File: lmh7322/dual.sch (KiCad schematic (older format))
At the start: 35 parts, among them U1 lmh7322

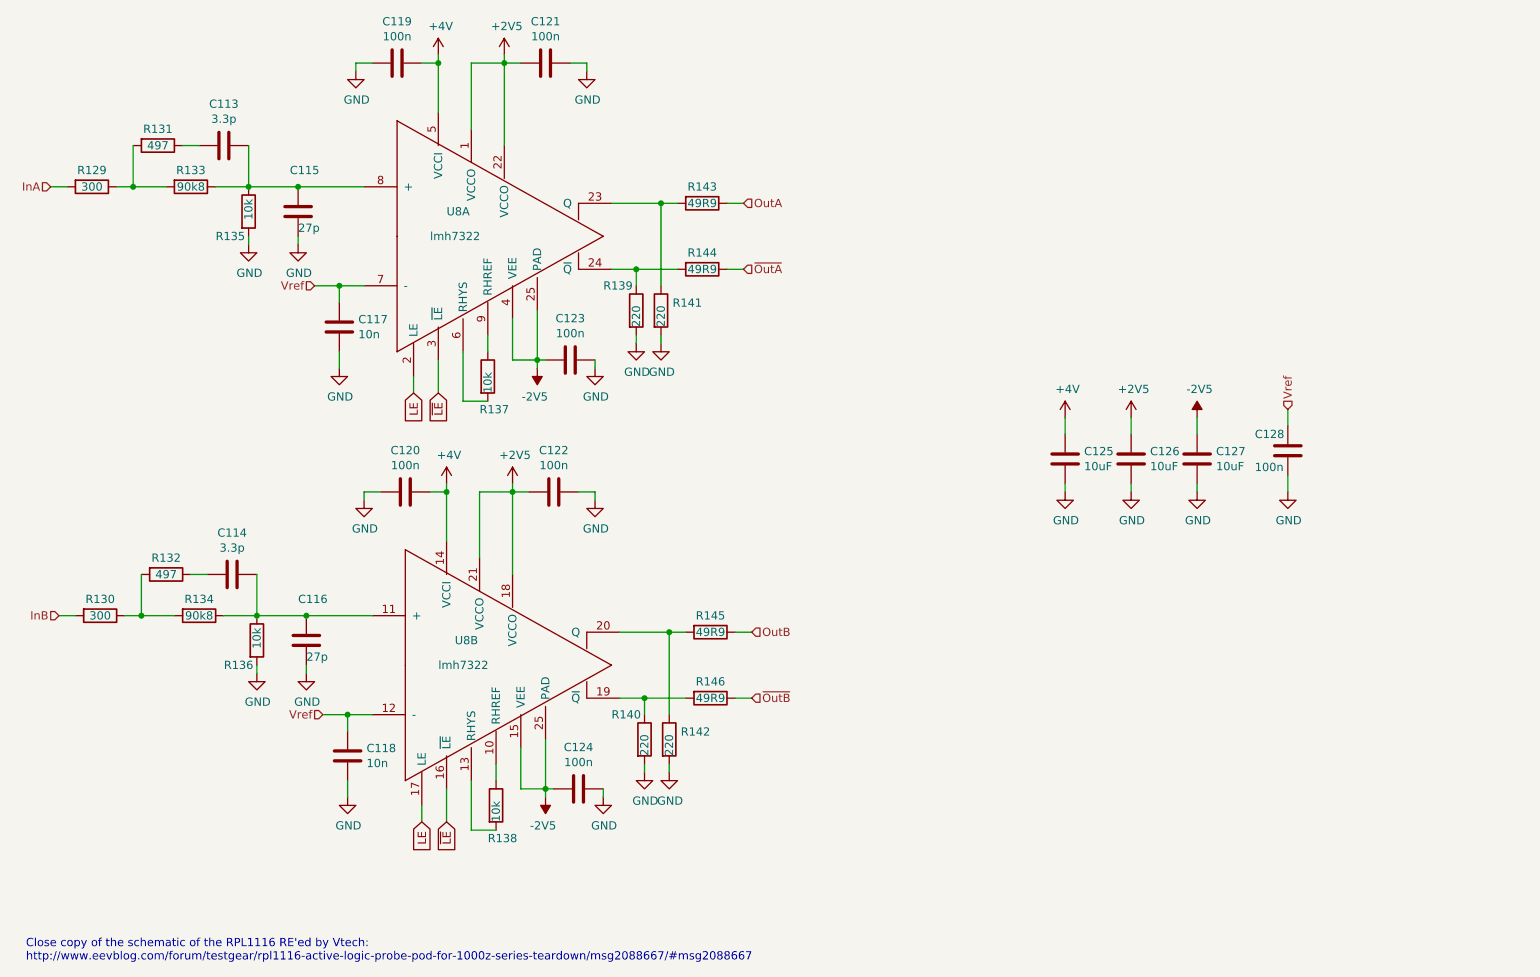
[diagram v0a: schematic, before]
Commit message: Use resistor arrays in the outputs
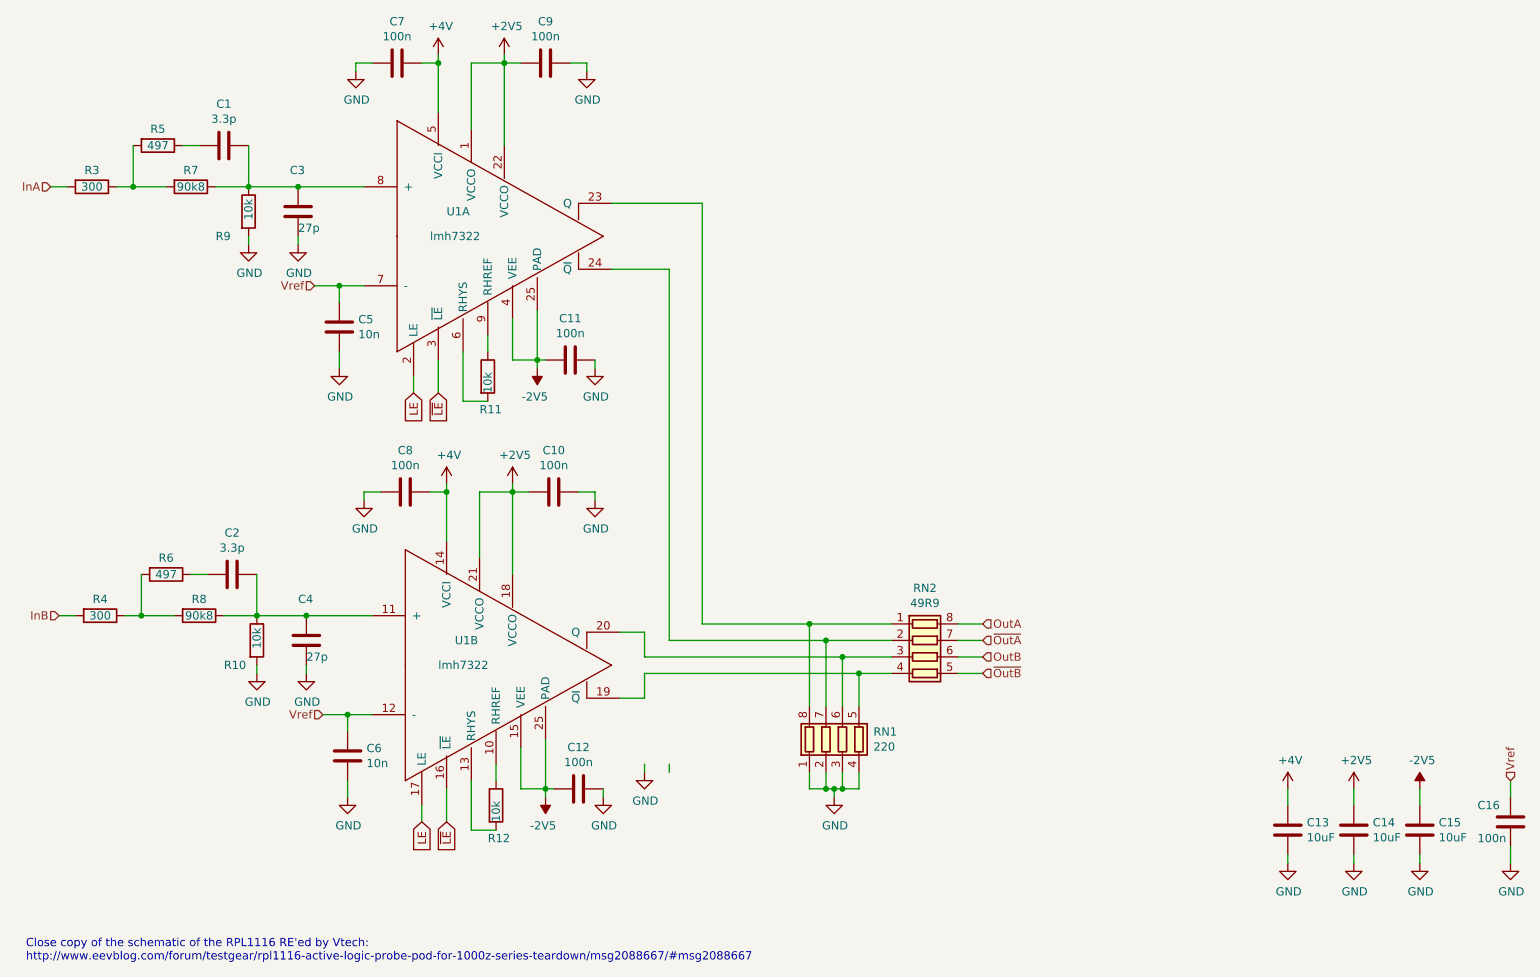
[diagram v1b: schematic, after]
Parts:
- removed R13, R14, R15, R16: 220, symbol Device:R
- removed R17, R18, R19, R20: 49R9, symbol Device:R
- added RN15: 220, symbol Device:R_Pack04
- added RN16: 49R9, symbol Device:R_Pack04
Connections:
- net GND: now also RN15.1 (R1.1), RN15.2 (R2.1), RN15.3 (R3.1), RN15.4 (R4.1)
- net OutA: now also RN16.8 (R1.2)
- net OutB: now also RN16.6 (R3.2)
- net ~OutA: now also RN16.7 (R2.2)
- net ~OutB: now also RN16.5 (R4.2)
- net at U1.23 (Q): now also RN15.8 (R1.2), RN16.1 (R1.1)
- net at U1.24 (~Q): now also RN15.7 (R2.2), RN16.2 (R2.1)
- net at U1.19 (~Q): now also RN15.5 (R4.2), RN16.4 (R4.1)
- net at U1.20 (Q): now also RN15.6 (R3.2), RN16.3 (R3.1)
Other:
- moved on the sheet: C13, C14, C15, C16

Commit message: Minor cleanup
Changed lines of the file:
@@
-$Comp
-L power:GND #PWR?
-U 1 1 5C467B73
-P 4900 5250
-AR Path="/5C467B73" Ref="#PWR?"  Part="1"
-AR Path="/5C4819A8/5C467B73" Ref="#PWR?"  Part="1"
-AR Path="/5C4C51E0/5C467B73" Ref="#PWR?"  Part="1"
-AR Path="/5C4E887D/5C467B73" Ref="#PWR?"  Part="1"
-AR Path="/5C4EBCE6/5C467B73" Ref="#PWR?"  Part="1"
-AR Path="/5C43A963/5C467B73" Ref="#PWR?"  Part="1"
-AR Path="/5C414CC7/5C467B73" Ref="#PWR039"  Part="1"
-AR Path="/5C4B42BD/5C467B73" Ref="#PWR068"  Part="1"
-AR Path="/5C4D3DE8/5C467B73" Ref="#PWR097"  Part="1"
-AR Path="/5C4DB186/5C467B73" Ref="#PWR0126"  Part="1"
-AR Path="/5C4E2524/5C467B73" Ref="#PWR0155"  Part="1"
-AR Path="/5C4E98BE/5C467B73" Ref="#PWR0184"  Part="1"
-AR Path="/5C4E98C7/5C467B73" Ref="#PWR0213"  Part="1"
-AR Path="/5C4E98D0/5C467B73" Ref="#PWR0242"  Part="1"
-F 0 "#PWR039" H 4900 5000 50  0001 C CNN
-F 1 "GND" H 4905 5077 50  0000 C CNN
-F 2 "" H 4900 5250 50  0001 C CNN
-F 3 "" H 4900 5250 50  0001 C CNN
-	1    4900 5250
-	1    0    0    -1
-$EndComp
 $Comp
 L power:GND #PWR?
@@
 	1    0    0    -1
 $EndComp
-Wire Wire Line
-	5050 5250 5050 5200
-Wire Wire Line
-	4900 5200 4900 5250
 Text HLabel 6950 4650 2    50   Input ~ 0
 ~OutB

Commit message: Started playing around with the PCB layout
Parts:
- removed C13, C14, C15: 10uF, symbol Device:C
- removed C16: 100n, symbol Device:C
- C1, C10, C11, C12, C2, C3, C4, C5, C6, C7, C8, C9: footprint (none) -> Capacitors_SMD.pretty:C_0603_HandSoldering
- R10, R11, R12, R3, R4, R5, R6, R7, R8, R9: footprint (none) -> Resistor_SMD:R_0603_1608Metric_Pad1.05x0.95mm_HandSolder
- RN15, RN16: footprint (none) -> Resistor_SMD:R_Array_Convex_4x0603
- U1: footprint (none) -> Package_DFN_QFN:QFN-24-1EP_4x4mm_P0.5mm_EP2.6x2.6mm_ThermalVias
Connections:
- net OutA: now also RN16.7 (R2.2); no longer RN16.8 (R1.2)
- net ~OutA: now also RN16.8 (R1.2); no longer RN16.7 (R2.2)
- net at RN15.8 (R1.2), RN16.1 (R1.1): now also U1.24 (~Q); no longer U1.23 (Q)
- net at RN15.7 (R2.2), RN16.2 (R2.1): now also U1.23 (Q); no longer U1.24 (~Q)

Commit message: Pre-clone
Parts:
- renumbered C1 to C201, C2 to C202, C3 to C203, C4 to C204, C5 to C205, C6 to C206, C7 to C207, C8 to C208, C9 to C209, C10 to C210, C11 to C211, C12 to C212, R3 to R201, R4 to R202, R5 to R203, R6 to R204, R7 to R205, R8 to R206, R9 to R207, R10 to R208, R11 to R209, R12 to R210, RN15 to RN901, RN16 to RN902, U1 to U201

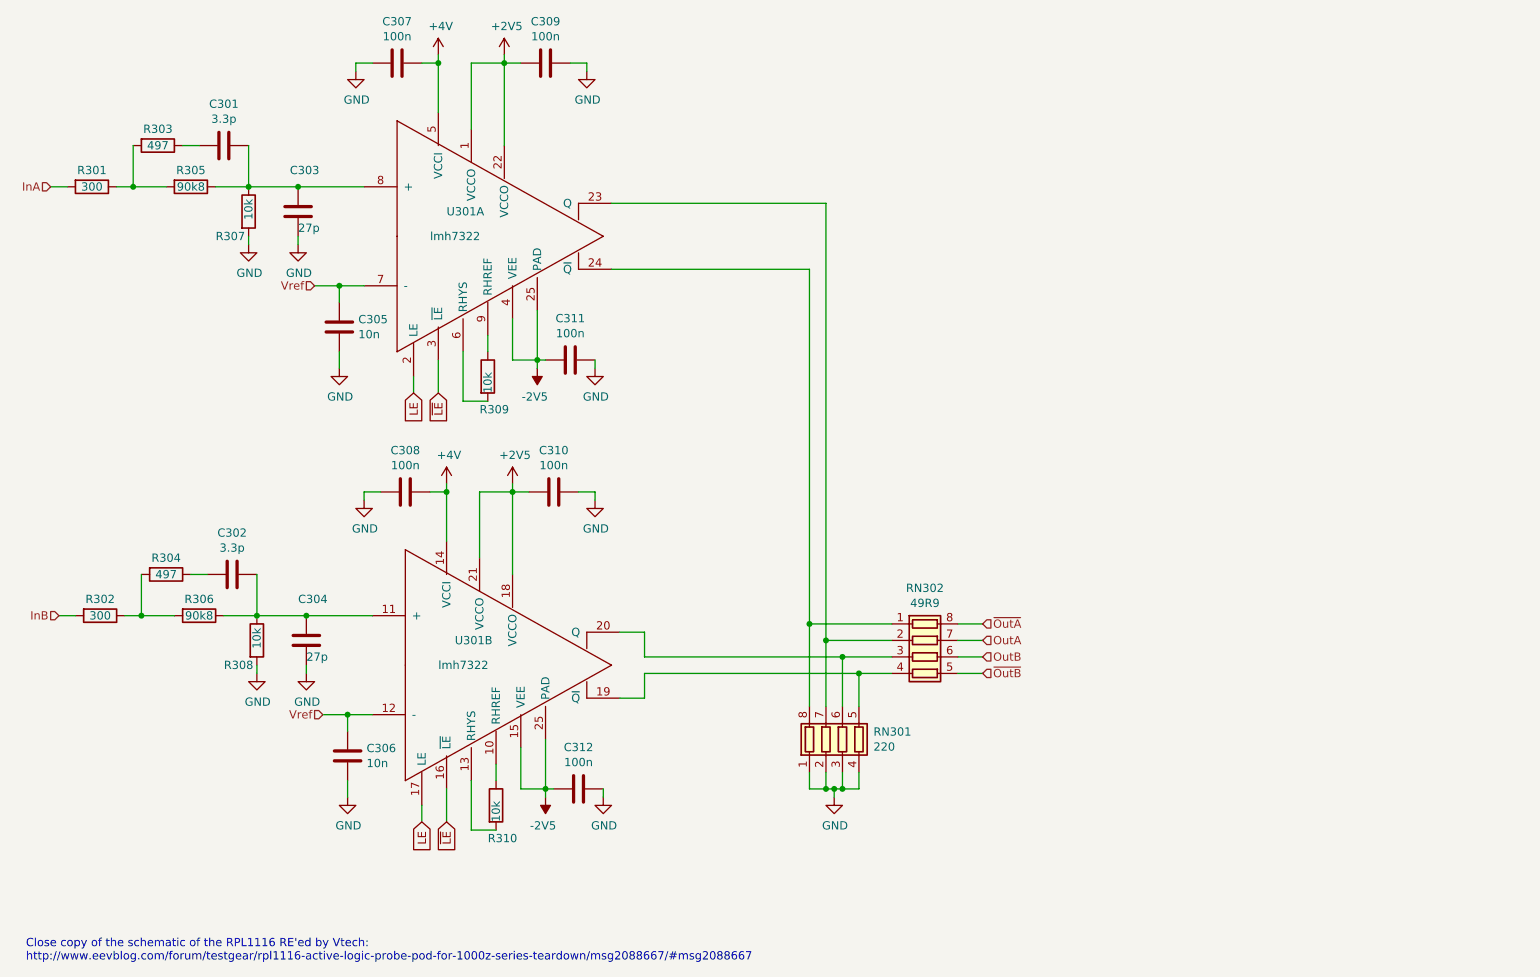
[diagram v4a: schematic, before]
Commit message: Finished the 4-layer single-sided board
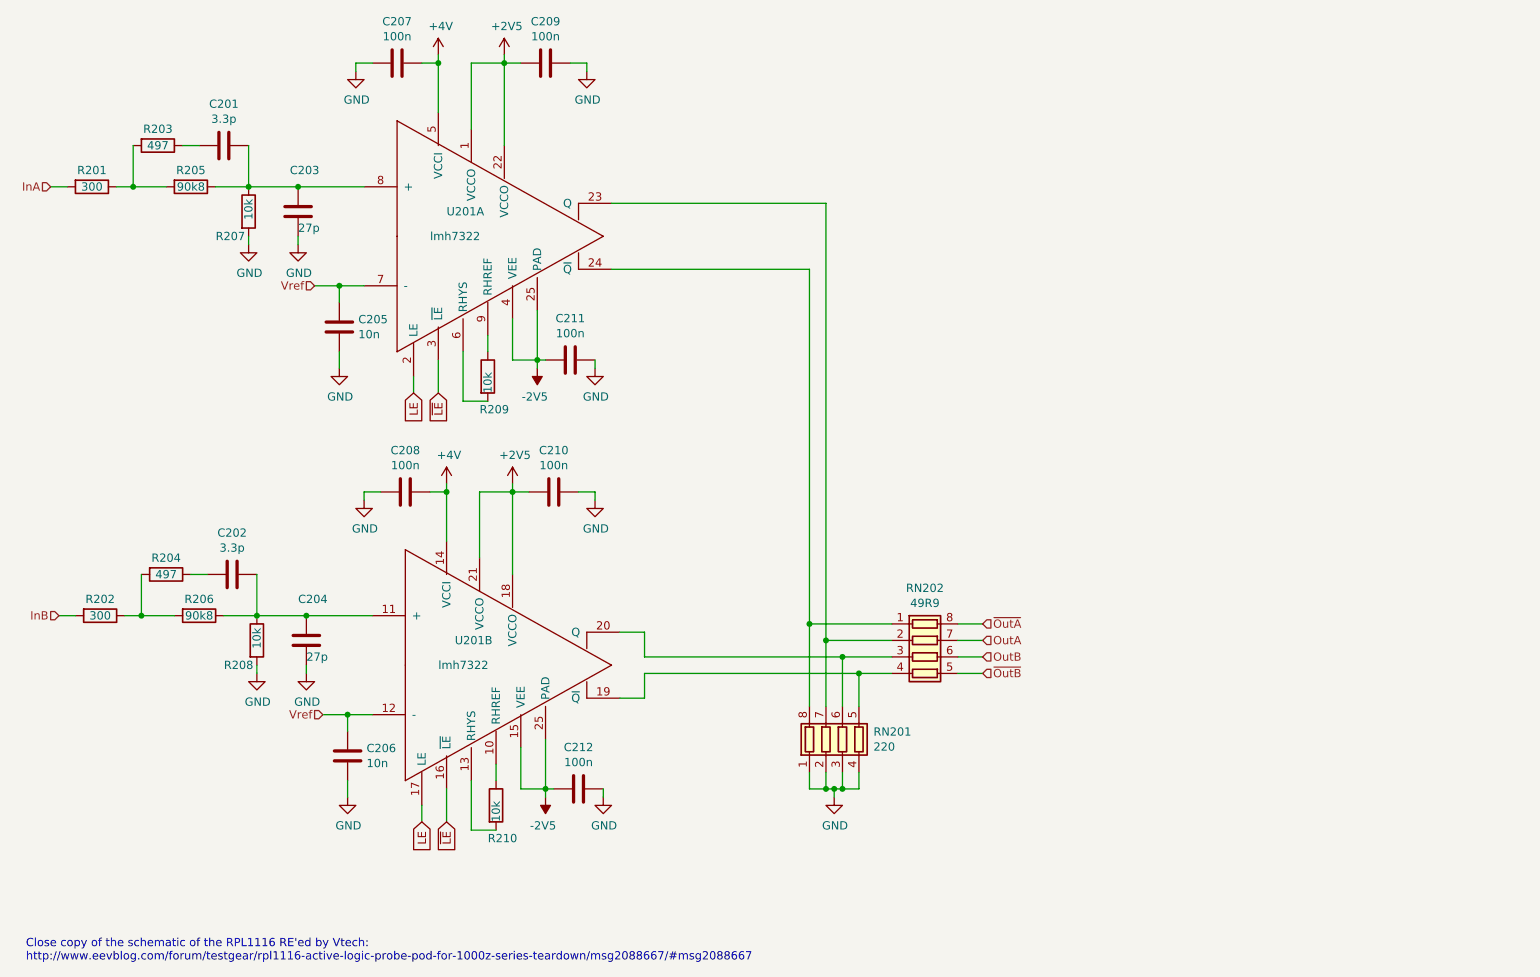
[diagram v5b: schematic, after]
